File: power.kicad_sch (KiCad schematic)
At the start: 15 parts, among them Q1001 DPLS350E, U1001 MC7805

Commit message: add export of symbol libray, edit symbol links
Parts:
- C1001: symbol enclosure:C_Polarized -> meas:C_Polarized
- C1003, C1005: symbol enclosure:C -> meas:C
- D1001: symbol enclosure:D_TVS -> meas:D_TVS
- D1002, D1004: symbol enclosure:D -> meas:D
- F1001: symbol enclosure:Fuse -> meas:Fuse
- F1002: symbol enclosure:Fuse_Socket_1 -> meas:Fuse_Socket_1
- Q1001: symbol enclosure:Q_PNP_BCE -> meas:Q_PNP_BCE
- R1001: symbol enclosure:R -> meas:R
- TP1001, TP1002, TP1007, TP1009: symbol enclosure:TestPoint -> meas:TestPoint
- U1001: symbol enclosure:MC7805 -> meas:MC7805
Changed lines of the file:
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@@
 	)
 	(symbol
-		(lib_id "power:+5VA")
+		(lib_id "meas:+5VA")
 		(at 227.33 82.55 0)
 		(unit 1)
@@
 	)
 	(symbol
-		(lib_id "enclosure:C_Polarized")
+		(lib_id "meas:C_Polarized")
 		(at 104.14 100.33 0)
 		(mirror y)
@@
 	)
 	(symbol
-		(lib_id "enclosure:D")
+		(lib_id "meas:D")
 		(at 208.28 99.06 0)
 		(unit 1)
@@
 	)
 	(symbol
-		(lib_id "enclosure:TestPoint")
+		(lib_id "meas:TestPoint")
 		(at 104.14 92.71 0)
 		(unit 1)
@@
 	)
 	(symbol
-		(lib_id "enclosure:+24V")
+		(lib_id "meas:+24V")
 		(at 170.18 82.55 0)
 		(unit 1)
@@
 	)
 	(symbol
-		(lib_id "enclosure:PWR_FLAG")
+		(lib_id "meas:PWR_FLAG")
 		(at 43.18 105.41 0)
 		(unit 1)
@@
 	)
 	(symbol
-		(lib_id "enclosure:GND")
+		(lib_id "meas:GND")
 		(at 43.18 107.95 0)
 		(unit 1)
@@
 	)
 	(symbol
-		(lib_id "enclosure:PWR_FLAG")
+		(lib_id "meas:PWR_FLAG")
 		(at 134.62 95.25 180)
 		(unit 1)
@@
 	)
 	(symbol
-		(lib_id "enclosure:PWR_FLAG")
+		(lib_id "meas:PWR_FLAG")
 		(at 196.85 111.76 0)
 		(unit 1)
@@
 	)
 	(symbol
-		(lib_id "enclosure:TestPoint")
+		(lib_id "meas:TestPoint")
 		(at 241.3 85.09 0)
 		(unit 1)
@@
 	)
 	(symbol
-		(lib_id "enclosure:D_TVS")
+		(lib_id "meas:D_TVS")
 		(at 55.88 100.33 90)
 		(unit 1)
@@
 	)
 	(symbol
-		(lib_id "enclosure:TestPoint")
+		(lib_id "meas:TestPoint")
 		(at 55.88 93.98 0)
 		(unit 1)
@@
 	)
 	(symbol
-		(lib_id "enclosure:Fuse")
+		(lib_id "meas:Fuse")
 		(at 81.28 93.98 90)
 		(unit 1)
@@
 	)
 	(symbol
-		(lib_id "enclosure:C")
+		(lib_id "meas:C")
 		(at 190.5 116.84 180)
 		(unit 1)
@@
 	)
 	(symbol
-		(lib_id "enclosure:TestPoint")
+		(lib_id "meas:TestPoint")
 		(at 55.88 106.68 180)
 		(unit 1)
@@
 	)
 	(symbol
-		(lib_id "enclosure:R")
+		(lib_id "meas:R")
 		(at 176.53 99.06 90)
 		(unit 1)
@@
 	)
 	(symbol
-		(lib_id "enclosure:MC7805")
+		(lib_id "meas:MC7805")
 		(at 208.28 111.76 0)
 		(unit 1)
@@
 	)
 	(symbol
-		(lib_id "enclosure:+24V")
+		(lib_id "meas:+24V")
 		(at 134.62 91.44 0)
 		(unit 1)
@@
 	(symbol
 		(lib_name "Fuse_Socket_1")
-		(lib_id "enclosure:Fuse_Socket_1")
+		(lib_id "meas:Fuse_Socket_1")
 		(at 81.28 93.98 270)
 		(unit 1)
@@
 	)
 	(symbol
-		(lib_id "enclosure:D")
+		(lib_id "meas:D")
 		(at 116.84 100.33 270)
 		(unit 1)
@@
 	)
 	(symbol
-		(lib_id "enclosure:Q_PNP_BCE")
+		(lib_id "meas:Q_PNP_BCE")
 		(at 190.5 88.9 270)
 		(mirror x)
@@
 	)
 	(symbol
-		(lib_id "enclosure:C")
+		(lib_id "meas:C")
 		(at 227.33 116.84 180)
 		(unit 1)
@@
 	)
 	(symbol
-		(lib_id "enclosure:GND")
+		(lib_id "meas:GND")
 		(at 208.28 124.46 0)
 		(unit 1)

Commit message: add export of footprint library, edit footprint links
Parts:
- C1001: footprint enclosure:CP_Elec_10x10 -> meas:CP_Elec_10x10
- C1003: footprint enclosure:C_0603_1608Metric_Pad1.08x0.95mm_HandSolder -> meas:C_0603_1608Metric_Pad1.08x0.95mm_HandSolder
- C1005: footprint enclosure:C_1210_3225Metric_Pad1.33x2.70mm_HandSolder -> meas:C_1210_3225Metric_Pad1.33x2.70mm_HandSolder
- D1001: footprint enclosure:D_SOD-323_HandSoldering -> meas:D_SOD-323_HandSoldering
- D1002, D1004: footprint enclosure:D_SOD-123 -> meas:D_SOD-123
- F1002: footprint enclosure:FuseHolder_Blade_ATO_Littelfuse_FLR_178.6165 -> meas:FuseHolder_Blade_ATO_Littelfuse_FLR_178.6165
- Q1001: footprint enclosure:SOT-223-3_TabPin2 -> meas:SOT-223-3_TabPin2
- R1001: footprint enclosure:R_1210_3225Metric_Pad1.30x2.65mm_HandSolder -> meas:R_1210_3225Metric_Pad1.30x2.65mm_HandSolder
- TP1001, TP1002, TP1007, TP1009: footprint enclosure:TP_0805_2012Metric -> meas:TP_0805_2012Metric
- U1001: footprint enclosure:TO-252-2 -> meas:TO-252-2
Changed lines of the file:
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@@
 			)
 		)
-		(property "Footprint" "enclosure:CP_Elec_10x10"
+		(property "Footprint" "meas:CP_Elec_10x10"
 			(at 103.1748 104.14 0)
 			(effects
@@
 			)
 		)
-		(property "Footprint" "enclosure:D_SOD-123"
+		(property "Footprint" "meas:D_SOD-123"
 			(at 208.28 99.06 0)
 			(effects
@@
 			)
 		)
-		(property "Footprint" "enclosure:TP_0805_2012Metric"
+		(property "Footprint" "meas:TP_0805_2012Metric"
 			(at 109.22 92.71 0)
 			(effects
@@
 			)
 		)
-		(property "Footprint" "enclosure:TP_0805_2012Metric"
+		(property "Footprint" "meas:TP_0805_2012Metric"
 			(at 246.38 85.09 0)
 			(effects
@@
 			)
 		)
-		(property "Footprint" "enclosure:D_SOD-323_HandSoldering"
+		(property "Footprint" "meas:D_SOD-323_HandSoldering"
 			(at 55.88 100.33 0)
 			(effects
@@
 			)
 		)
-		(property "Footprint" "enclosure:TP_0805_2012Metric"
+		(property "Footprint" "meas:TP_0805_2012Metric"
 			(at 60.96 93.98 0)
 			(effects
@@
 			)
 		)
-		(property "Footprint" "enclosure:C_0603_1608Metric_Pad1.08x0.95mm_HandSolder"
+		(property "Footprint" "meas:C_0603_1608Metric_Pad1.08x0.95mm_HandSolder"
 			(at 189.5348 113.03 0)
 			(effects
@@
 			)
 		)
-		(property "Footprint" "enclosure:TP_0805_2012Metric"
+		(property "Footprint" "meas:TP_0805_2012Metric"
 			(at 50.8 106.68 0)
 			(effects
@@
 			)
 		)
-		(property "Footprint" "enclosure:R_1210_3225Metric_Pad1.30x2.65mm_HandSolder"
+		(property "Footprint" "meas:R_1210_3225Metric_Pad1.30x2.65mm_HandSolder"
 			(at 176.53 100.838 90)
 			(effects
@@
 			)
 		)
-		(property "Footprint" "enclosure:TO-252-2"
+		(property "Footprint" "meas:TO-252-2"
 			(at 208.915 115.57 0)
 			(effects
@@
 			)
 		)
-		(property "Footprint" "enclosure:FuseHolder_Blade_ATO_Littelfuse_FLR_178.6165"
+		(property "Footprint" "meas:FuseHolder_Blade_ATO_Littelfuse_FLR_178.6165"
 			(at 81.28 92.202 90)
 			(effects
@@
 			)
 		)
-		(property "Footprint" "enclosure:D_SOD-123"
+		(property "Footprint" "meas:D_SOD-123"
 			(at 116.84 100.33 0)
 			(effects
@@
 			)
 		)
-		(property "Footprint" "enclosure:SOT-223-3_TabPin2"
+		(property "Footprint" "meas:SOT-223-3_TabPin2"
 			(at 193.04 83.82 0)
 			(effects
@@
 			)
 		)
-		(property "Footprint" "enclosure:C_1210_3225Metric_Pad1.33x2.70mm_HandSolder"
+		(property "Footprint" "meas:C_1210_3225Metric_Pad1.33x2.70mm_HandSolder"
 			(at 226.3648 113.03 0)
 			(effects

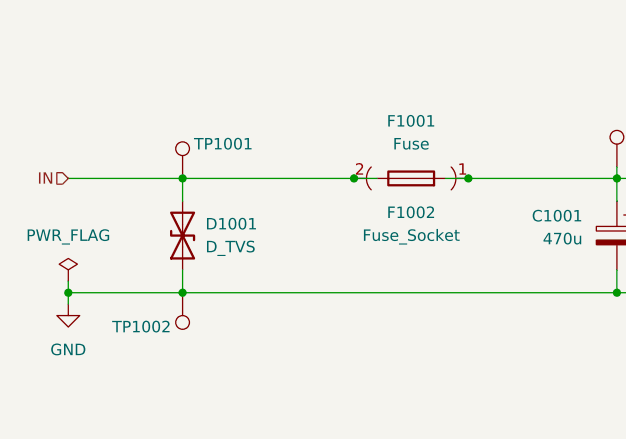
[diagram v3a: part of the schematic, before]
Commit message: add interconnect layout
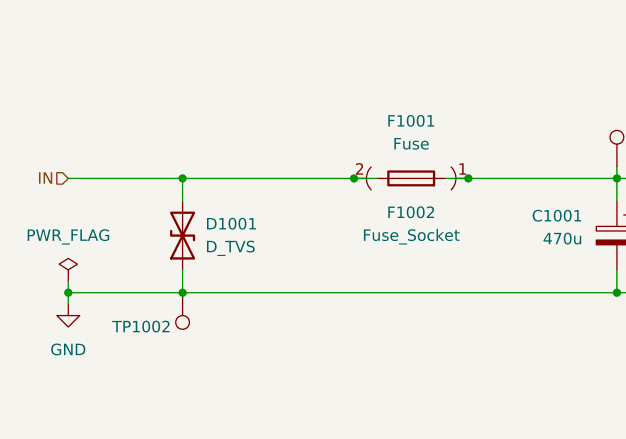
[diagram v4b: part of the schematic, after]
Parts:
- removed TP1001: ~, meas:TP_0805_2012Metric, symbol meas:TestPoint
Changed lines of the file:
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@@
-	)
-	(symbol
-		(lib_id "meas:TestPoint")
-		(at 55.88 93.98 0)
-		(unit 1)
-		(exclude_from_sim no)
-		(in_bom yes)
-		(on_board yes)
-		(dnp no)
-		(property "Reference" "TP1001"
-			(at 57.15 90.17 0)
-			(effects
-				(font
-					(size 1.27 1.27)
-				)
-				(justify left)
-			)
-		)
-		(property "Value" "~"
-			(at 58.42 91.9479 0)
-			(effects
-				(font
-					(size 1.27 1.27)
-				)
-				(justify left)
-			)
-		)
-		(property "Footprint" "meas:TP_0805_2012Metric"
-			(at 60.96 93.98 0)
-			(effects
-				(font
-					(size 1.27 1.27)
-				)
-				(hide yes)
-			)
-		)
-		(property "Datasheet" "./datasheet/RCTCTE.pdf"
-			(at 60.96 93.98 0)
-			(effects
-				(font
-					(size 1.27 1.27)
-				)
-				(hide yes)
-			)
-		)
-		(property "Description" "test point"
-			(at 55.88 93.98 0)
-			(effects
-				(font
-					(size 1.27 1.27)
-				)
-				(hide yes)
-			)
-		)
-		(property "MPN" "RCTCTE"
-			(at 55.88 93.98 0)
-			(effects
-				(font
-					(size 1.27 1.27)
-				)
-				(hide yes)
-			)
-		)
-		(property "VPN" "660-RCTCTE"
-			(at 55.88 93.98 0)
-			(effects
-				(font
-					(size 1.27 1.27)
-				)
-				(hide yes)
-			)
-		)
-		(pin "1"
-		)
-		(instances
-			(project "enclosure"
-				(path "/8ec0899b-9d7b-491d-933a-49b74b34a0df/f6df2627-821f-46ca-b36c-d1d3b4f0e28f"
-					(reference "TP1001")
-					(unit 1)
-				)
-			)
-			(project "meas"
-				(path "/f710e4da-f895-4fe1-9122-3234febe82c7/722db133-dd98-4c12-99f4-3c9027a3ce09"
-					(reference "TP1001")
-					(unit 1)
-				)
-			)
-		)
 	)
 	(symbol
